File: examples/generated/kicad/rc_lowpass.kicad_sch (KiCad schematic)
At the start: 3 parts

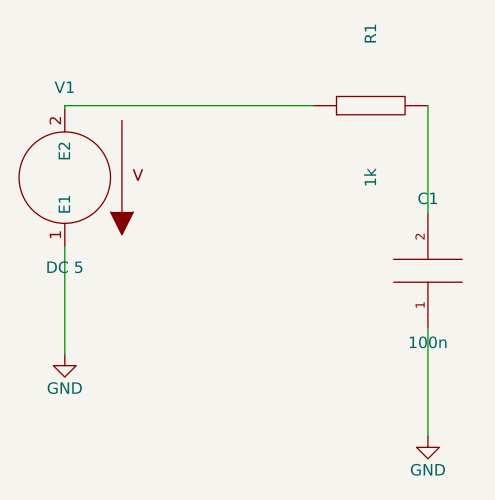
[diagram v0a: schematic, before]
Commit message: Ensure connectivity matches, as measured by opamp connectivity.
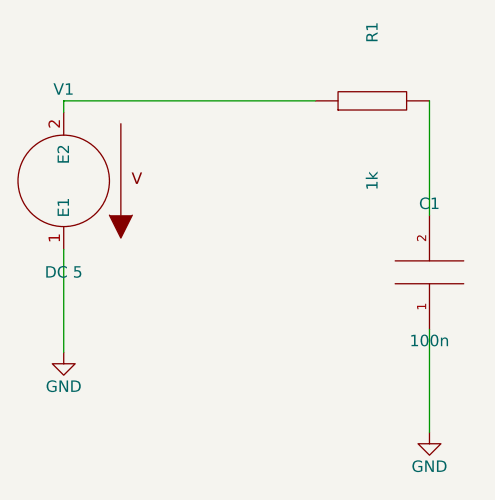
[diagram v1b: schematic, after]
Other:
- moved on the sheet: R1
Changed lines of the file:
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@@
     (comment 1 "Generated by mixedsig2cad")
   )
-  (symbol (lib_id "VSOURCE") (at 56.00 86.00 180) (unit 1)
+  (symbol (lib_id "VSOURCE") (at 55.88 86.36 180) (unit 1)
     (in_bom yes) (on_board yes)
-    (property "Reference" "V1" (at 56.0 76.0 0)
+    (property "Reference" "V1" (at 55.88 76.2 0)
       (effects (font (size 1.27 1.27)))
     )
-    (property "Value" "DC 5" (at 56.0 96.0 0)
+    (property "Value" "DC 5" (at 55.88 96.52 0)
       (effects (font (size 1.27 1.27)))
     )
@@
     )
   )
-  (symbol (lib_id "GND") (at 56.00 105.62 0) (unit 1)
+  (symbol (lib_id "GND") (at 55.88 105.41 0) (unit 1)
     (in_bom yes) (on_board yes)
-    (property "Reference" "#PWR0001" (at 56.0 101.81 0)
+    (property "Reference" "#PWR0001" (at 55.88 101.6 0)
       (effects (font (size 1.27 1.27)) hide)
     )
-    (property "Value" "GND" (at 56.0 109.43 0)
+    (property "Value" "GND" (at 55.88 109.22 0)
       (effects (font (size 1.27 1.27)))
     )
@@
     )
   )
-  (symbol (lib_id "R") (at 90.00 78.00 90) (unit 1)
+  (symbol (lib_id "R") (at 90.17 77.47 90) (unit 1)
     (in_bom yes) (on_board yes)
-    (property "Reference" "R1" (at 90.0 70.0 0)
+    (property "Reference" "R1" (at 90.17 69.85 0)
       (effects (font (size 1.27 1.27)))
     )
-    (property "Value" "1k" (at 90.0 86.0 0)
+    (property "Value" "1k" (at 90.17 86.36 0)
       (effects (font (size 1.27 1.27)))
     )
@@
     )
   )
-  (symbol (lib_id "CAP") (at 96.35 96.35 180) (unit 1)
+  (symbol (lib_id "CAP") (at 96.52 96.52 180) (unit 1)
     (in_bom yes) (on_board yes)
-    (property "Reference" "C1" (at 96.35 88.35 0)
+    (property "Reference" "C1" (at 96.52 88.9 0)
       (effects (font (size 1.27 1.27)))
     )
-    (property "Value" "100n" (at 96.35 104.35 0)
+    (property "Value" "100n" (at 96.52 104.14 0)
       (effects (font (size 1.27 1.27)))
     )
@@
     )
   )
-  (symbol (lib_id "GND") (at 96.35 114.70 0) (unit 1)
+  (symbol (lib_id "GND") (at 96.52 114.30 0) (unit 1)
     (in_bom yes) (on_board yes)
-    (property "Reference" "#PWR0002" (at 96.35 110.89 0)
+    (property "Reference" "#PWR0002" (at 96.52 110.49 0)
       (effects (font (size 1.27 1.27)) hide)
     )
-    (property "Value" "GND" (at 96.35 118.51 0)
+    (property "Value" "GND" (at 96.52 118.11 0)
       (effects (font (size 1.27 1.27)))
     )
@@
     )
   )
-  (wire (pts (xy 96.35 102.70) (xy 96.35 114.70))
+  (wire (pts (xy 96.52 102.87) (xy 96.52 114.30))
     (stroke (width 0) (type solid) (color 0 0 0 0))
   )
-  (wire (pts (xy 56.00 93.62) (xy 56.00 105.62))
+  (wire (pts (xy 55.88 93.98) (xy 55.88 105.41))
     (stroke (width 0) (type solid) (color 0 0 0 0))
   )
-  (wire (pts (xy 56.00 78.38) (xy 56.00 78.00))
+  (wire (pts (xy 55.88 78.74) (xy 55.88 77.47))
     (stroke (width 0) (type solid) (color 0 0 0 0))
   )
-  (wire (pts (xy 56.00 78.00) (xy 83.65 78.00))
+  (wire (pts (xy 55.88 77.47) (xy 83.82 77.47))
     (stroke (width 0) (type solid) (color 0 0 0 0))
   )
-  (wire (pts (xy 96.35 78.00) (xy 96.35 90.00))
+  (wire (pts (xy 96.52 77.47) (xy 96.52 90.17))
     (stroke (width 0) (type solid) (color 0 0 0 0))
   )

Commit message: Refactor further.
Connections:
- net vin: now reaches R1.1, V1.2 (E2)
- net vout: now reaches C1.2, R1.2
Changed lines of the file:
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@@
     )
+  )
+  (label "vin" (at 69.85 77.47 0)
+    (effects (font (size 1.27 1.27)))
+  )
+  (label "vout" (at 96.52 77.47 0)
+    (effects (font (size 1.27 1.27)))
   )
   (wire (pts (xy 96.52 102.87) (xy 96.52 114.30))

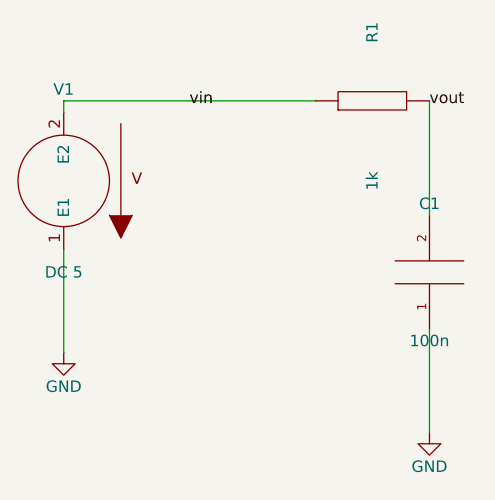
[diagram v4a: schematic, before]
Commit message: Fix CMOS inverter issue.
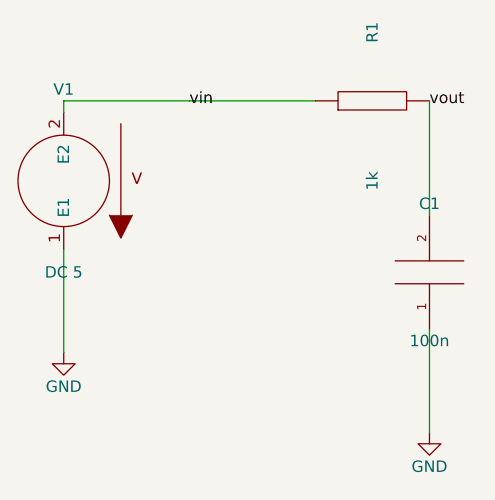
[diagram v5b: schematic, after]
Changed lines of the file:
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@@
     (stroke (width 0) (type solid) (color 0 0 0 0))
   )
-  (wire (pts (xy 55.88 77.47) (xy 83.82 77.47))
+  (wire (pts (xy 55.88 77.47) (xy 69.85 77.47))
     (stroke (width 0) (type solid) (color 0 0 0 0))
   )
-  (wire (pts (xy 96.52 77.47) (xy 96.52 90.17))
+  (wire (pts (xy 83.82 77.47) (xy 69.85 77.47))
     (stroke (width 0) (type solid) (color 0 0 0 0))
   )
+  (wire (pts (xy 96.52 90.17) (xy 96.52 77.47))
+    (stroke (width 0) (type solid) (color 0 0 0 0))
+  )

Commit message: Manually change schematics to match what I want.
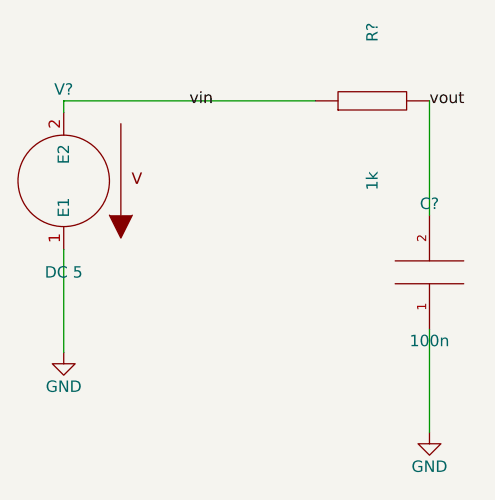
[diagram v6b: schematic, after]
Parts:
- renumbered C1 to C?, R1 to R?, V1 to V?

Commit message: Attempt to match manual schematics with seeded layout and generation.
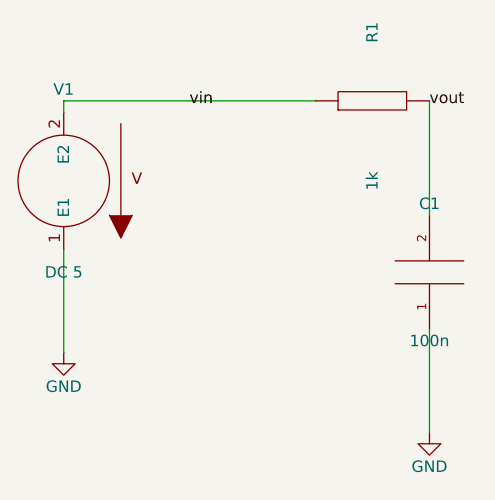
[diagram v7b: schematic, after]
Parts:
- gave numbers to parts that had none: 3
